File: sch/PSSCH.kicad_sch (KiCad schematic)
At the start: 17 parts, among them J10 Conn_01x04_Male, Q1 BC817, Q2 BC817, U2 SI2301DS, U3 SI2301DS, U4 Mini360, U5 Mini360

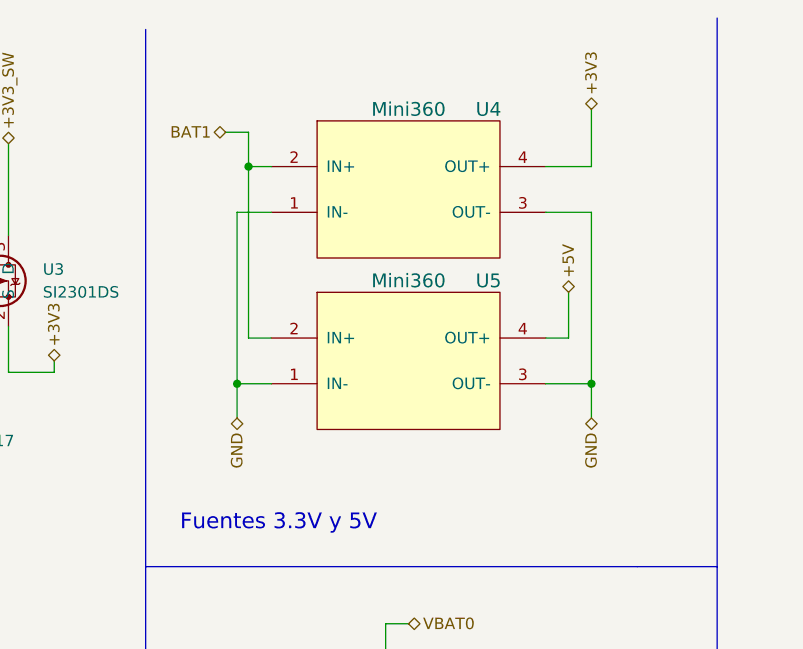
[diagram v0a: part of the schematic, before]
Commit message: Diseño actualizado - MK4
Diseño actualizado para cumplir con la nueva misión. Se elimino una placa, el sensor de calidad de aire, servos y sensor de humedad
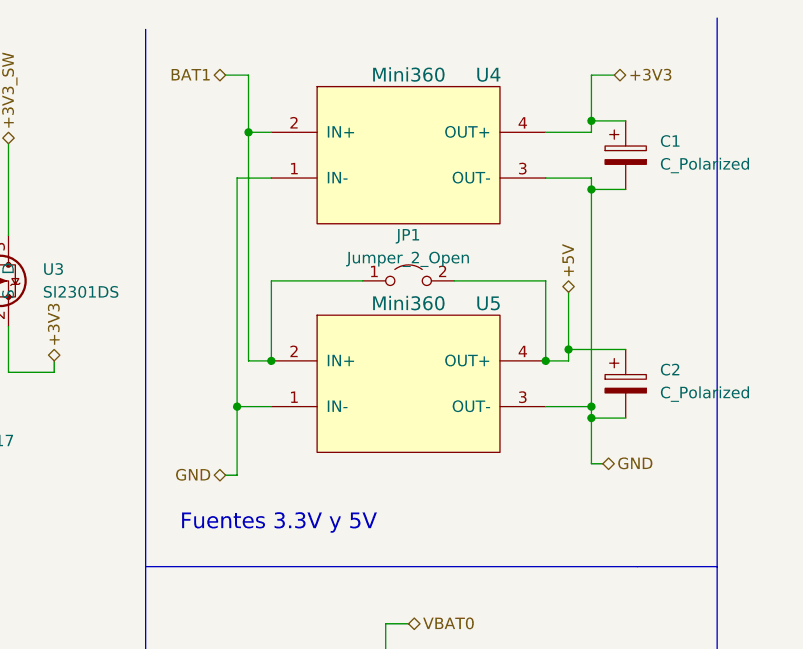
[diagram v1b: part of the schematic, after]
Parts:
- added C1, C2: C_Polarized, Capacitor_Tantalum_SMD:CP_EIA-6032-15_Kemet-U_Pad2.25x2.35mm_HandSolder, symbol Device:C_Polarized
- added JP1: Jumper_2_Open, Jumper:SolderJumper-2_P1.3mm_Open_RoundedPad1.0x1.5mm, symbol Jumper:Jumper_2_Open
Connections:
- net +3V3: now also C1.1
- net +5V: now also C2.1, JP1.2 (B)
- net BAT1: now also JP1.1 (A)
- net GND: now also C1.2, C2.2
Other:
- moved on the sheet: U4, U5
